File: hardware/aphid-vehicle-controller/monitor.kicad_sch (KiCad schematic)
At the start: 16 parts, among them J4 SWD, U7 STM32G431KBTx, Y2 8 MHz

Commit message: Worked on VC PCB
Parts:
- removed J4: SWD, Connector:Tag-Connect_TC2030-IDC-FP_2x03_P1.27mm_Vertical, symbol Connector:Conn_ARM_SWD_TagConnect_TC2030
- added J5: MONITOR_DEBUG, Connector_PinHeader_1.27mm:PinHeader_2x07_P1.27mm_Vertical_SMD, symbol Connector:Conn_ST_STDC14
- added J6: SWD, Connector:Tag-Connect_TC2030-IDC-FP_2x03_P1.27mm_Vertical, symbol Connector:Conn_ARM_SWD_TagConnect_TC2030
- renumbered C41 to C43, C42 to C44, C43 to C45, C44 to C46, C45 to C47, C46 to C48, C47 to C49, C48 to C50
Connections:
- net +3.3V: now also J5.3 (VCC), J6.1 (VCC)
- net GND: now also J5.11 (GNDDetect), J5.5 (GND), J5.7 (GND), J6.5 (GND)
- net MONITOR_DBG_RX: now also J5.13 (VCP_RX)
- net MONITOR_DBG_TX: now also J5.14 (VCP_TX)
- net MONITOR_NRST: now also J5.12 (~{RST}), J6.3 (~{RESET})
- net MONITOR_SWCLK: now also J5.6 (JCLK/SWCLK), J6.4 (SWCLK)
- net MONITOR_SWDIO: now also J5.4 (JTMS/SWDIO), J6.2 (SWDIO)
- net MONITOR_SWO: now also J5.8 (JTDO/SWO), J6.6 (SWO)
- no-connect marks 0 -> 2
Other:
- moved on the sheet: C50, D10, R17, R18

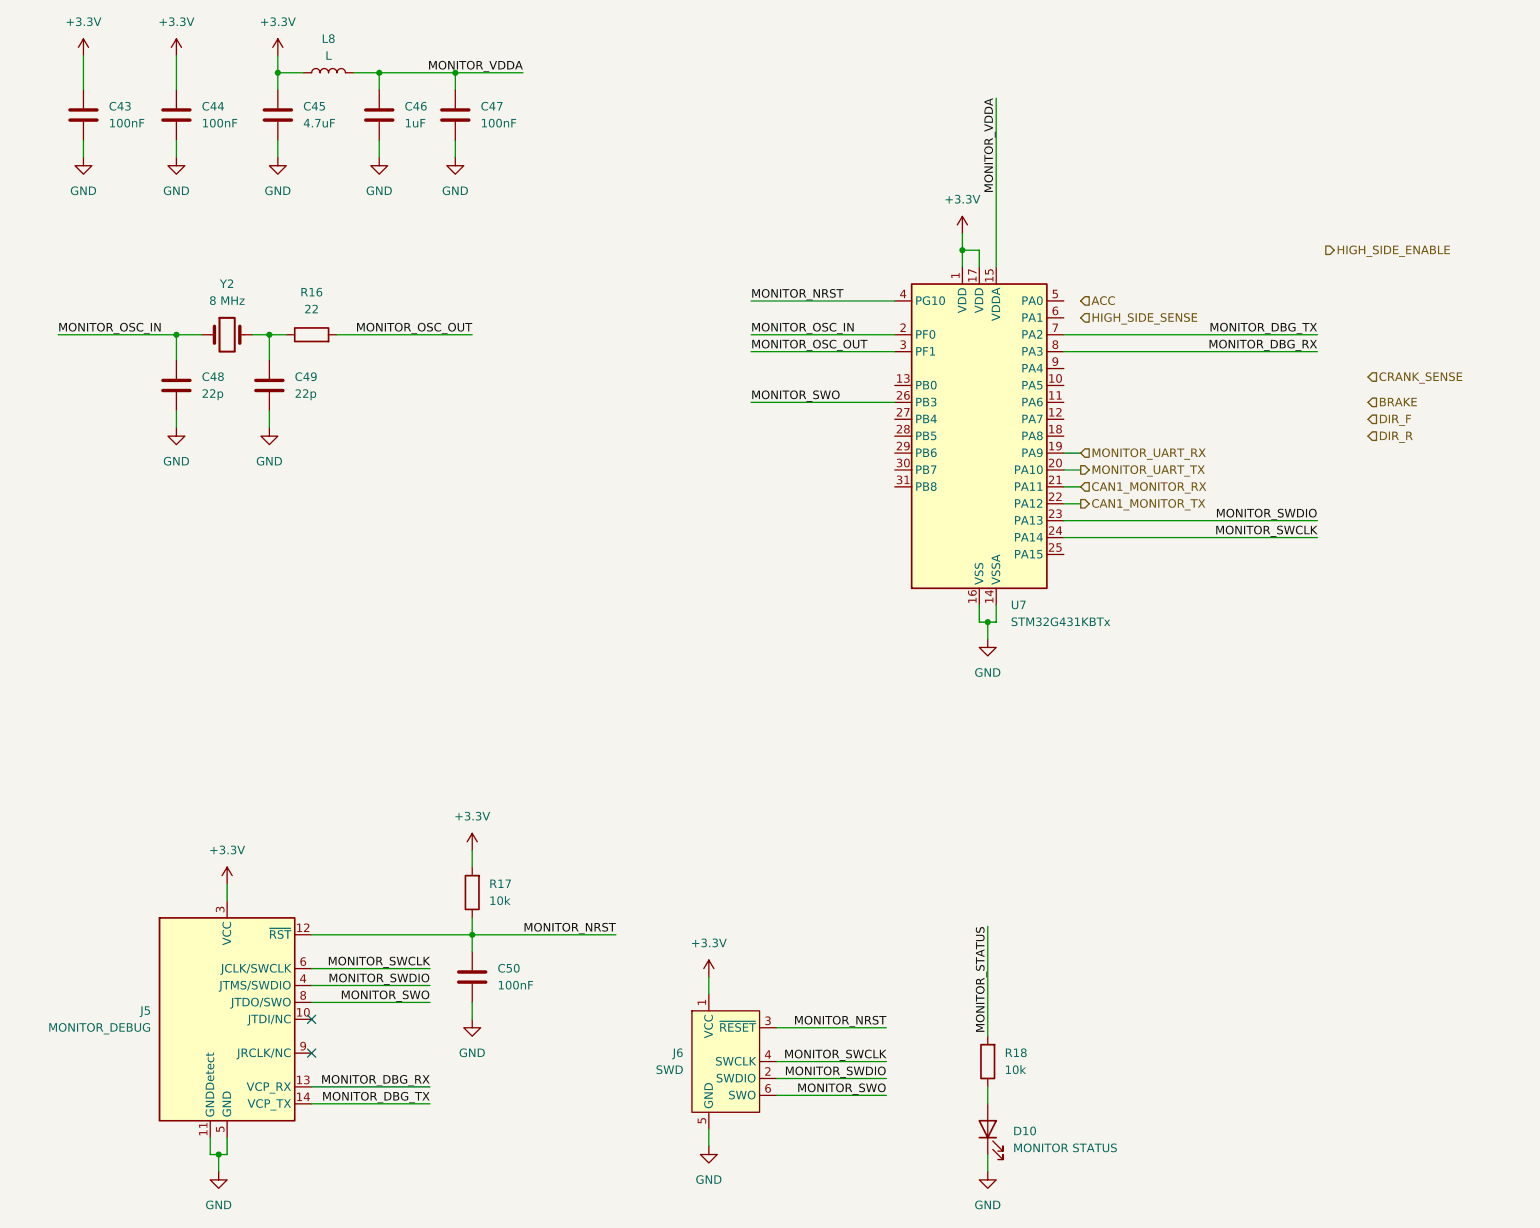
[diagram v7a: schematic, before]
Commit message: ERC check passing
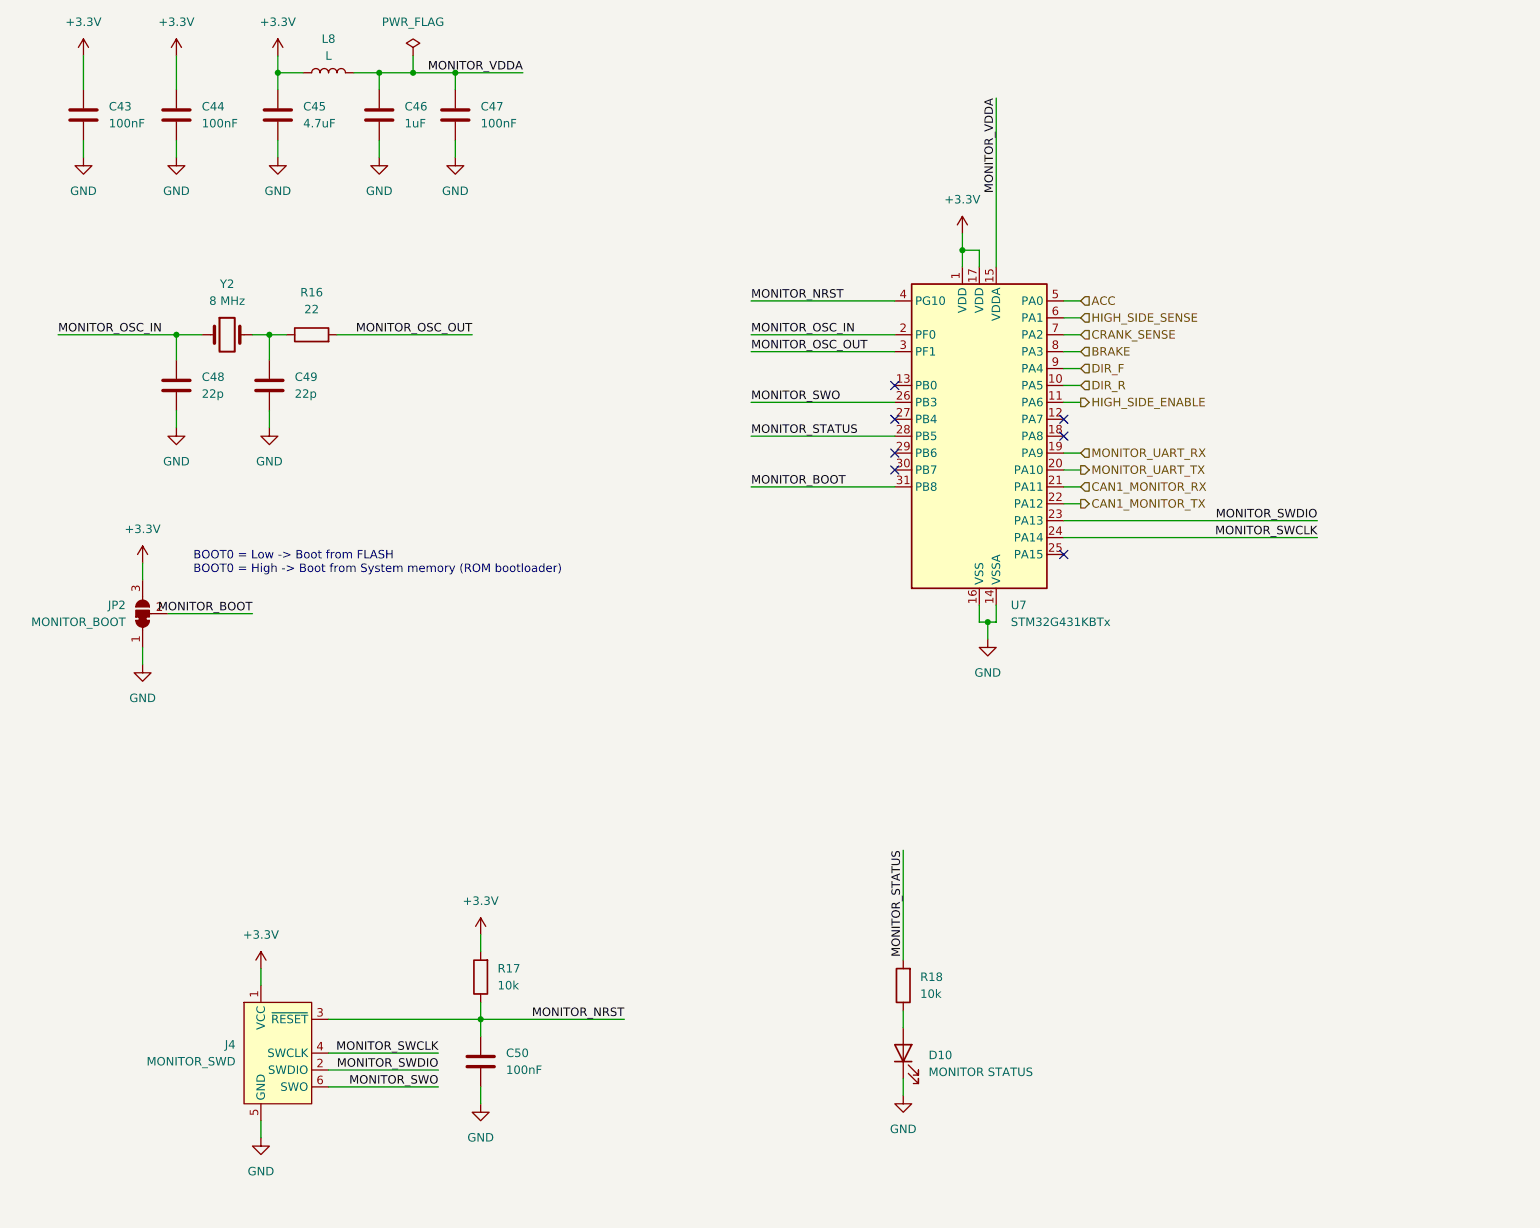
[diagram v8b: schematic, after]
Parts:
- removed J5: MONITOR_DEBUG, Connector_PinHeader_1.27mm:PinHeader_2x07_P1.27mm_Vertical_SMD, symbol Connector:Conn_ST_STDC14
- added JP2: MONITOR_BOOT, symbol Jumper:SolderJumper_3_Bridged12
- J4: renamed from J6; value SWD -> MONITOR_SWD
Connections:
- net MONITOR_DBG_RX is gone; now on net BRAKE: U7.8 (PA3)
- net MONITOR_DBG_TX is gone; now on net CRANK_SENSE: U7.7 (PA2)
- net +3.3V: now also JP2.3 (B)
- net ACC: now also U7.5 (PA0)
- net DIR_F: now also U7.9 (PA4)
- net DIR_R: now also U7.10 (PA5)
- net GND: now also JP2.1 (A)
- net HIGH_SIDE_ENABLE: now also U7.11 (PA6)
- net HIGH_SIDE_SENSE: now also U7.6 (PA1)
- net MONITOR_STATUS: now also U7.28 (PB5)
- net MONITOR_BOOT: now reaches U7.31 (PB8)
- net MONITOR_BOOT: now also JP2.2 (C)
- no-connect marks 2 -> 7
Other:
- note added: "BOOT0 = Low -> Boot from FLASH BOOT0 = High -> Boot from System memory (ROM bootloader)"
- moved on the sheet: C50, D10, J4, R17, R18
